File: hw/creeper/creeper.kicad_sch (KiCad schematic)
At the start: 17 parts, among them SW1 EG1218, U1 ATtiny85V-10SU, U2 LIS2DH12TR

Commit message: feat(pcb): v0.7
* added TC2030_AVR pogo debug plug connector
* added isolating resistors to stabilize ISP
* fixed missing connections of battery holder
* added 0R bridge for always-on w/o switch
* moved mounting hole out of case opening
* did manual place and route
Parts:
- added J1: TC2030_AVR, PCM_marbastlib-various:CON_TC2030_outlined, symbol PCM_marbastlib-various:TC2030_AVR
- added RDEC_MISO1, RDEC_MOSI1, RDEC_RST1, RDEC_SCK1: 100R, Resistor_SMD:R_0603_1608Metric_Pad0.98x0.95mm_HandSolder, symbol Device:R_Small
- added R_AON1: 0R, Resistor_SMD:R_0603_1608Metric_Pad0.98x0.95mm_HandSolder, symbol Device:R_Small
- renumbered RPU4 to RPU_CS1, RPU1 to RPU_RST1, RPU3 to RPU_SCL1, RPU2 to RPU_SDA1, R1 to R_BUZ1, R2 to R_LED1, R3 to R_LED2
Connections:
- net +3V: now also J1.2 (VCC), R_AON1.1
- net GND: now also J1.6 (GND); no longer U2.3 (SDO/SA0)
- net INT: now also RDEC_SCK1.1
- net SCL: now also RDEC_MISO1.1
- net SDA: now also RDEC_MOSI1.1
- net ~RESET: now reaches RPU_RST1.1, U1.1 (~{RESET}/PB5)
- net ~RESET: now also RDEC_RST1.1
- net at BT1.1 (+), C_PWR1.1, SW1.3: now also R_AON1.2
- new net: J1.1 (MISO), RDEC_MISO1.2
- new net: J1.4 (MOSI), RDEC_MOSI1.2
- new net: J1.5 (~{RST}), RDEC_RST1.2
- new net: J1.3 (SCK), RDEC_SCK1.2
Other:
- note added: "0.7"
- note added: "2025-AUG-20"
- note removed: "0.6"
- note removed: "2025-JUL-16"
- moved on the sheet: RPU_CS1, RPU_SCL1, RPU_SDA1

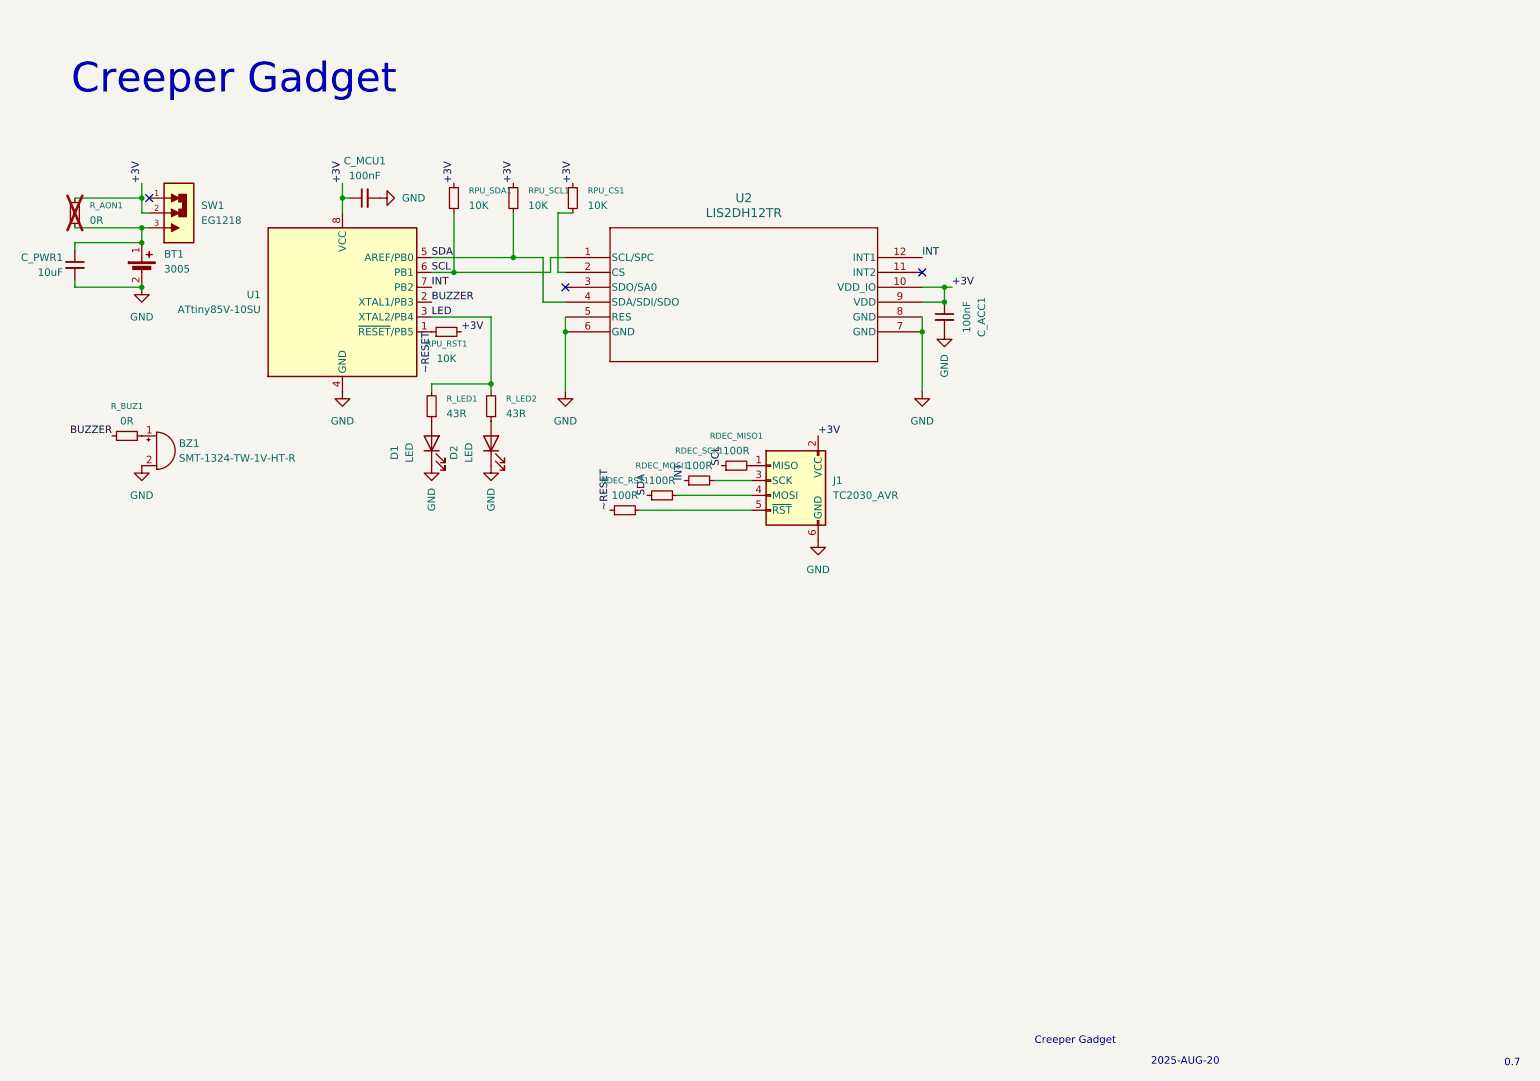
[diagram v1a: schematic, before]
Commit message: feat: rev. 0.10: use analog switch for programmer isolation
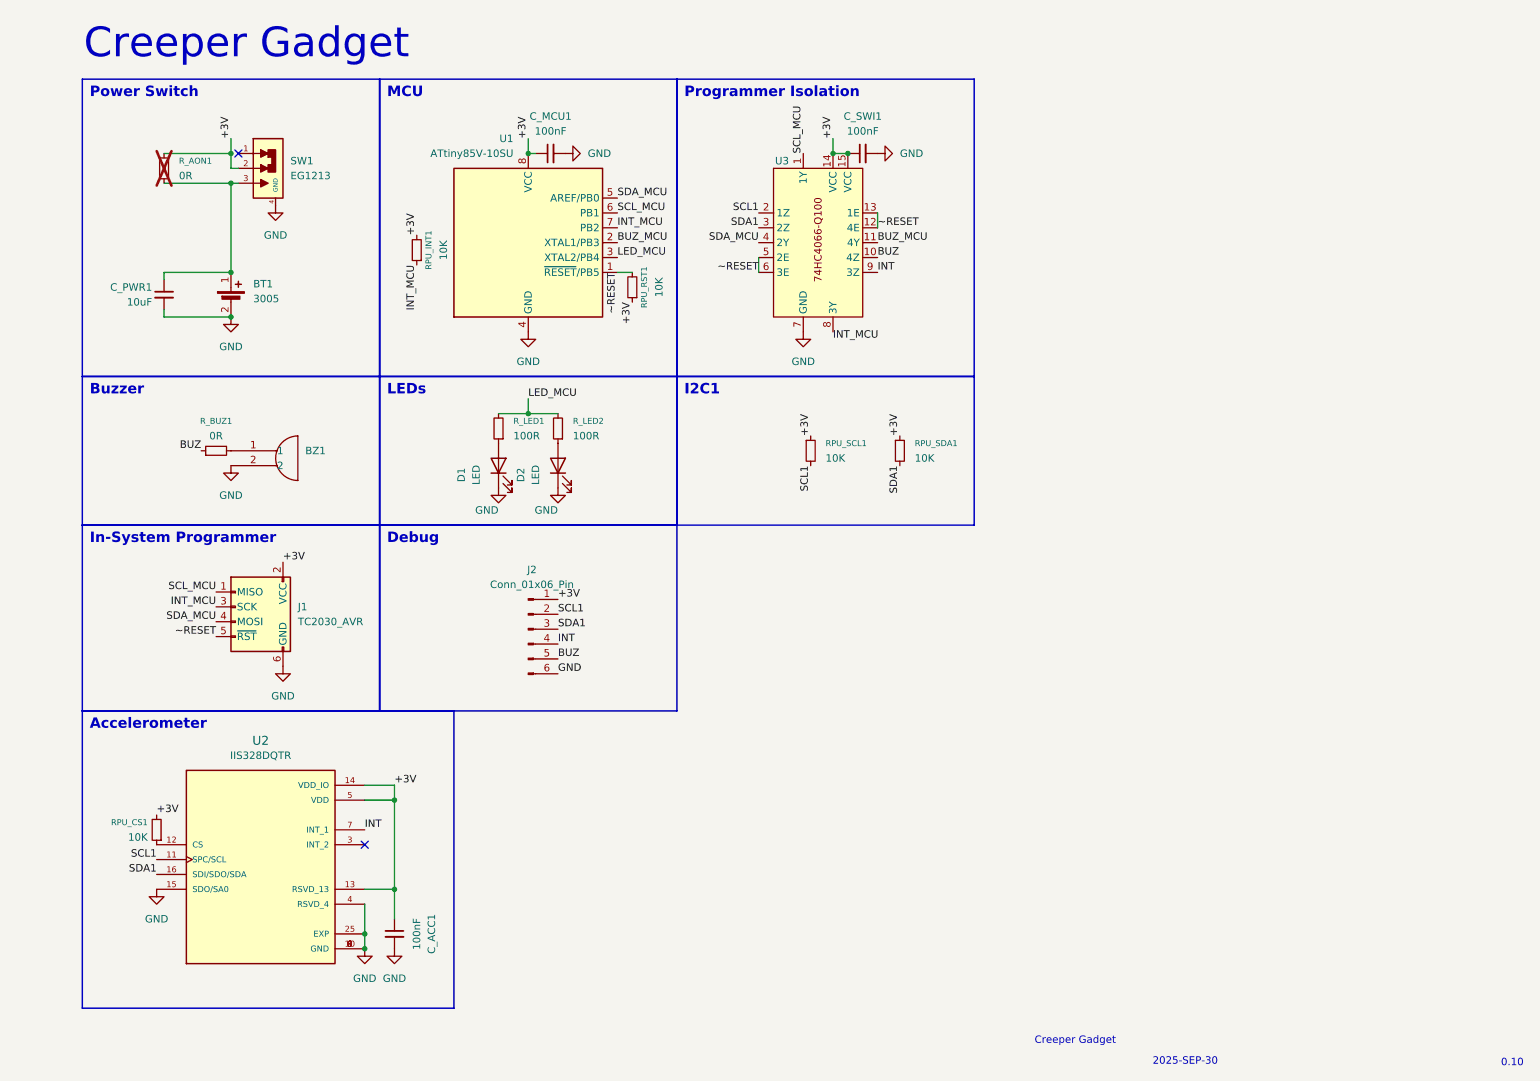
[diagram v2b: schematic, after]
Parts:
- removed RDEC_MISO1, RDEC_MOSI1, RDEC_RST1, RDEC_SCK1: 100R, Resistor_SMD:R_0603_1608Metric_Pad0.98x0.95mm_HandSolder, symbol Device:R_Small
- added C_SWI1: 100nF, creeper:C_0603_1608Metric_Pad1.08x0.95mm_HandSolder, symbol Device:C_Small
- added J2: Conn_01x06_Pin, creeper:PinHeader_1x06_P2.54mm_Vertical, symbol Connector:Conn_01x06_Pin
- added RPU_INT1: 10K, creeper:R_0603_1608Metric_Pad0.98x0.95mm_HandSolder, symbol Device:R_Small
- added U3: ~, creeper:QFN50P300X250X100-15N, symbol creeper:74HC4066-Q100
- BZ1: value SMT-1324-TW-1V-HT-R -> ~; footprint creeper:XDCR_SMT-1324-TW-1V-HT-R -> creeper:XDCR_SMT-0825-S-2-R; symbol Device:Buzzer -> creeper:PT-1241PFQ; MPN SMT-1324-TW-1V-HT-R -> (none); Manufacturer PUI Audio, Inc. -> (none); SolderJoints 2 -> (none)
- C_ACC1, C_MCU1: footprint Capacitor_SMD:C_0603_1608Metric_Pad1.08x0.95mm_HandSolder -> creeper:C_0603_1608Metric_Pad1.08x0.95mm_HandSolder
- C_PWR1: footprint Capacitor_SMD:C_0805_2012Metric_Pad1.18x1.45mm_HandSolder -> creeper:C_0805_2012Metric_Pad1.18x1.45mm_HandSolder
- RPU_CS1, RPU_RST1, RPU_SCL1, RPU_SDA1, R_AON1, R_BUZ1: footprint Resistor_SMD:R_0603_1608Metric_Pad0.98x0.95mm_HandSolder -> creeper:R_0603_1608Metric_Pad0.98x0.95mm_HandSolder
- R_LED1, R_LED2: value 43R -> 100R; footprint Resistor_SMD:R_0603_1608Metric_Pad0.98x0.95mm_HandSolder -> creeper:R_0603_1608Metric_Pad0.98x0.95mm_HandSolder
- SW1: value EG1218 -> EG1213; footprint creeper:SW_EG1218 -> creeper:SW_EG1213; symbol creeper:EG1218 -> creeper:EG1213
- U1: footprint Package_SO:SOIC-8_5.3x5.3mm_P1.27mm -> creeper:SOIC-8_5.3x5.3mm_P1.27mm
- U2: value LIS2DH12TR -> IIS328DQTR; footprint creeper:LGA-12_STM -> creeper:IIS328DQTR_QFN50P400X400X185-25N; symbol creeper:LIS2DH12TR -> creeper:IIS328DQTR; A_MAX (none) -> 1.85; B_MAX (none) -> 0.3; B_MIN (none) -> 0.2; B_NOM (none) -> 0.25; Check_prices (none) -> https://www.snapeda.com/parts/IIS328DQTR/STMicroelectronics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; D2_NOM (none) -> 2.3; D_MAX (none) -> 4.0; D_MIN (none) -> 4.0; D_NOM (none) -> 4.0; Description_1 (none) -> Accelerometer X, Y, Z Axis ±2g, 4g, 8g 25Hz ~ 500Hz 24-QFN 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; DigiKey_Part_Number (none) -> 497-15701-1-ND; E2_NOM (none) -> 2.3; ENOM (none) -> 0.5; E_MAX (none) -> 4.0; E_MIN (none) -> 4.0; E_NOM (none) -> 4.0; L_MAX (none) -> 0.45; L_MIN (none) -> 0.35; L_NOM (none) -> 0.4; MANUFACTURER (none) -> ST Microelectronics; MAXIMUM_PACKAGE_HEIGHT (none) -> 1.85mm; MF (none) -> STMicroelectronics; MP (none) -> IIS328DQTR; MPN LIS2DH12TR -> (none); Manufacturer STMicroelectronics -> (none); PARTREV (none) -> 3; PIN_COUNT_D (none) -> 6.0; PIN_COUNT_E (none) -> 6.0; Package (none) -> QFN-24 STMicroelectronics; STANDARD (none) -> IPC 7351B; SnapEDA_Link (none) -> https://www.snapeda.com/parts/IIS328DQTR/STMicroelectronics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; SolderJoints 12 -> (none)
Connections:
- net +3V: now also RPU_CS1.2, RPU_RST1.1, U2.13 (RSVD_13), U2.14 (VDD_IO), U2.5 (VDD), C_SWI1.1, J2.1 (Pin_1), RPU_INT1.2, U3.14 (VCC), U3.15 (VCC); no longer RPU_CS1.1, RPU_RST1.2, U2.10 (VDD_IO), U2.9 (VDD)
- net GND: now also SW1.4 (GND), U2.10 (GND), U2.15 (SDO/SA0), U2.25 (EXP), U2.4 (RSVD_4), U2.9 (GND), C_SWI1.2, J2.6 (Pin_6), U3.7 (GND); no longer U2.5 (RES), U2.7 (GND)
- net INT: now also U2.7 (INT_1), J2.4 (Pin_4), U3.9 (3Z); no longer U1.7 (PB2), U2.12 (INT1)
- net ~RESET: now also J1.5 (~{RST}), RPU_RST1.2, U3.12 (4E), U3.13 (1E), U3.5 (2E), U3.6 (3E); no longer RPU_RST1.1
- net SCL_MCU: now reaches J1.1 (MISO)
- net SCL_MCU: now also U1.6 (PB1), U3.1 (1Y)
- net SDA_MCU: now reaches J1.4 (MOSI)
- net SDA_MCU: now also U1.5 (AREF/PB0), U3.4 (2Y)
- net INT_MCU: now reaches J1.3 (SCK)
- net INT_MCU: now also U1.7 (PB2), RPU_INT1.1, U3.8 (3Y)
- net SCL1: now reaches U2.11 (SPC/SCL)
- net SCL1: now also RPU_SCL1.2, J2.2 (Pin_2), U3.2 (1Z)
- net BUZZER renamed BUZ
- net BUZ: now also J2.5 (Pin_5), U3.10 (4Z); no longer U1.2 (XTAL1/PB3)
- net LED renamed LED_MCU
- removed net SCL: RPU_SDA1.2, U1.6 (PB1), U2.1 (SCL/SPC)
- removed net SDA: RPU_SCL1.2, U1.5 (AREF/PB0), U2.4 (SDA/SDI/SDO)
- new net: RPU_CS1.1, U2.12 (CS)
- new net BUZ_MCU: U1.2 (XTAL1/PB3), U3.11 (4Y)
- new net SDA1: J2.3 (Pin_3), RPU_SDA1.2, U2.16 (SDI/SDO/SDA), U3.3 (2Z)
- no-connect marks 3 -> 2
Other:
- note added: "0.10"
- note added: "2025-SEP-30"
- note added: "Accelerometer"
- note added: "Buzzer"
- note added: "Debug"
- note added: "I2C1"
- note added: "In-System Programmer"
- note added: "LEDs"
- note added: "MCU"
- note added: "Power Switch"
- note added: "Programmer Isolation"
- note removed: "0.7"
- note removed: "2025-AUG-20"
- moved on the sheet: BT1, C_ACC1, C_MCU1, C_PWR1, D1, D2, J1, RPU_CS1, RPU_RST1, RPU_SCL1, RPU_SDA1, R_AON1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

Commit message: feat: v0.11: replace accelerometer with optional spring vibration sensor
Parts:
- added RPU_SVS1: 10K, creeper:R_0603_1608Metric_Pad0.98x0.95mm_HandSolder, symbol Device:R
- added SVS1: SW_Push, creeper:SW_180xxP_Spring_Vibration_Sensor, symbol Switch:SW_Push
- BZ1, J1, R_AON1: now left out of the parts list
- J2: now not fitted; now left out of the parts list
- SW1: Check_prices https://www.snapeda.com/parts/EG1218/E-Switch/view-part/?re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 -> https://www.snapeda.com/parts/EG1213/E-Switch/view-part/?re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; MP EG1218 -> EG1213; MPN EG1218 -> EG1213; PURCHASE-URL https://pricing.snapeda.com/search/part/EG1218/?ref=eda -> https://pricing.snapeda.com/search/part/EG1213/?ref=eda; SnapEDA_Link https://www.snapeda.com/parts/EG1218/E-Switch/view-part/?re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 -> https://www.snapeda.com/parts/EG1213/E-Switch/view-part/?re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; SolderJoints (none) -> 5
- U2: MANUFACTURER ST Microelectronics -> (none); MPN (none) -> IIS328DQTR; Manufacturer (none) -> ST Microelectronics; SolderJoints (none) -> 25; now not fitted
- U3: MPN (none) -> 74HC4066BQ-Q100,11; Manufacturer (none) -> Nexperia USA Inc.; SolderJoints (none) -> 15; now not fitted
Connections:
- net +3V: now also RPU_SVS1.2
- net INT: now also SVS1.1
- new net: RPU_SVS1.1, SVS1.2
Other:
- note added: "0.11"
- note added: "2025-OCT-19"
- note added: "Spring vibration sensor"
- note removed: "0.10"
- note removed: "2025-SEP-30"
- moved on the sheet: RPU_SCL1, RPU_SDA1

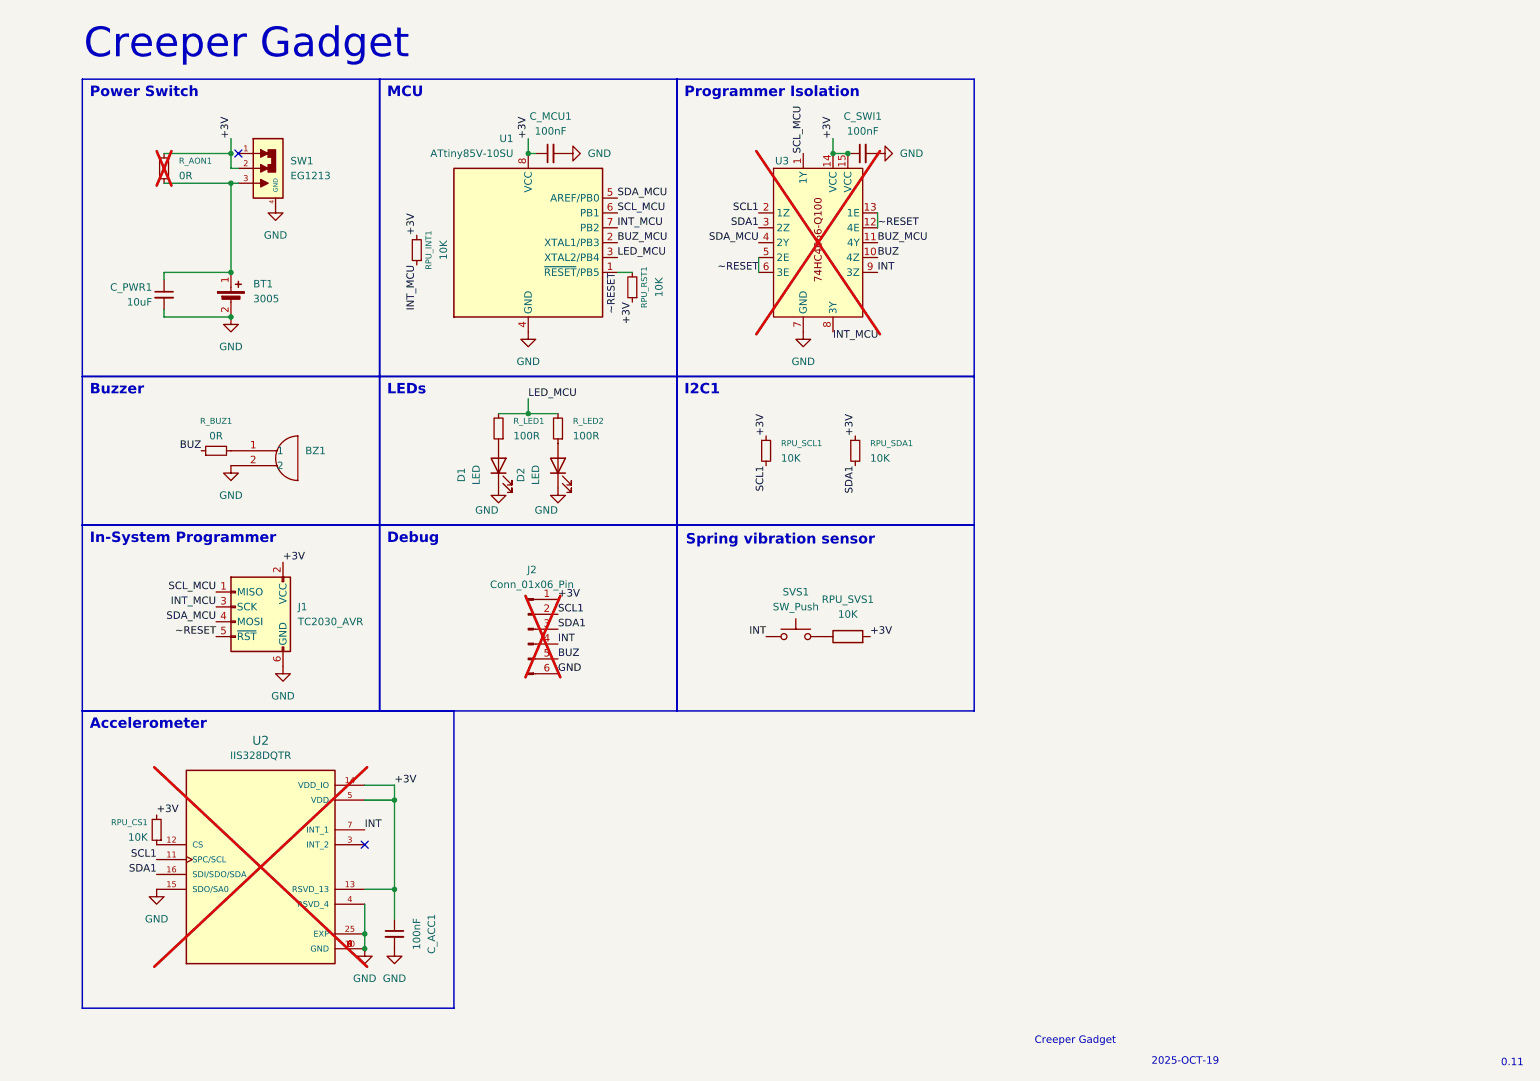
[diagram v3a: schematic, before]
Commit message: fix(sch+pcb): update footprints, reset DNP
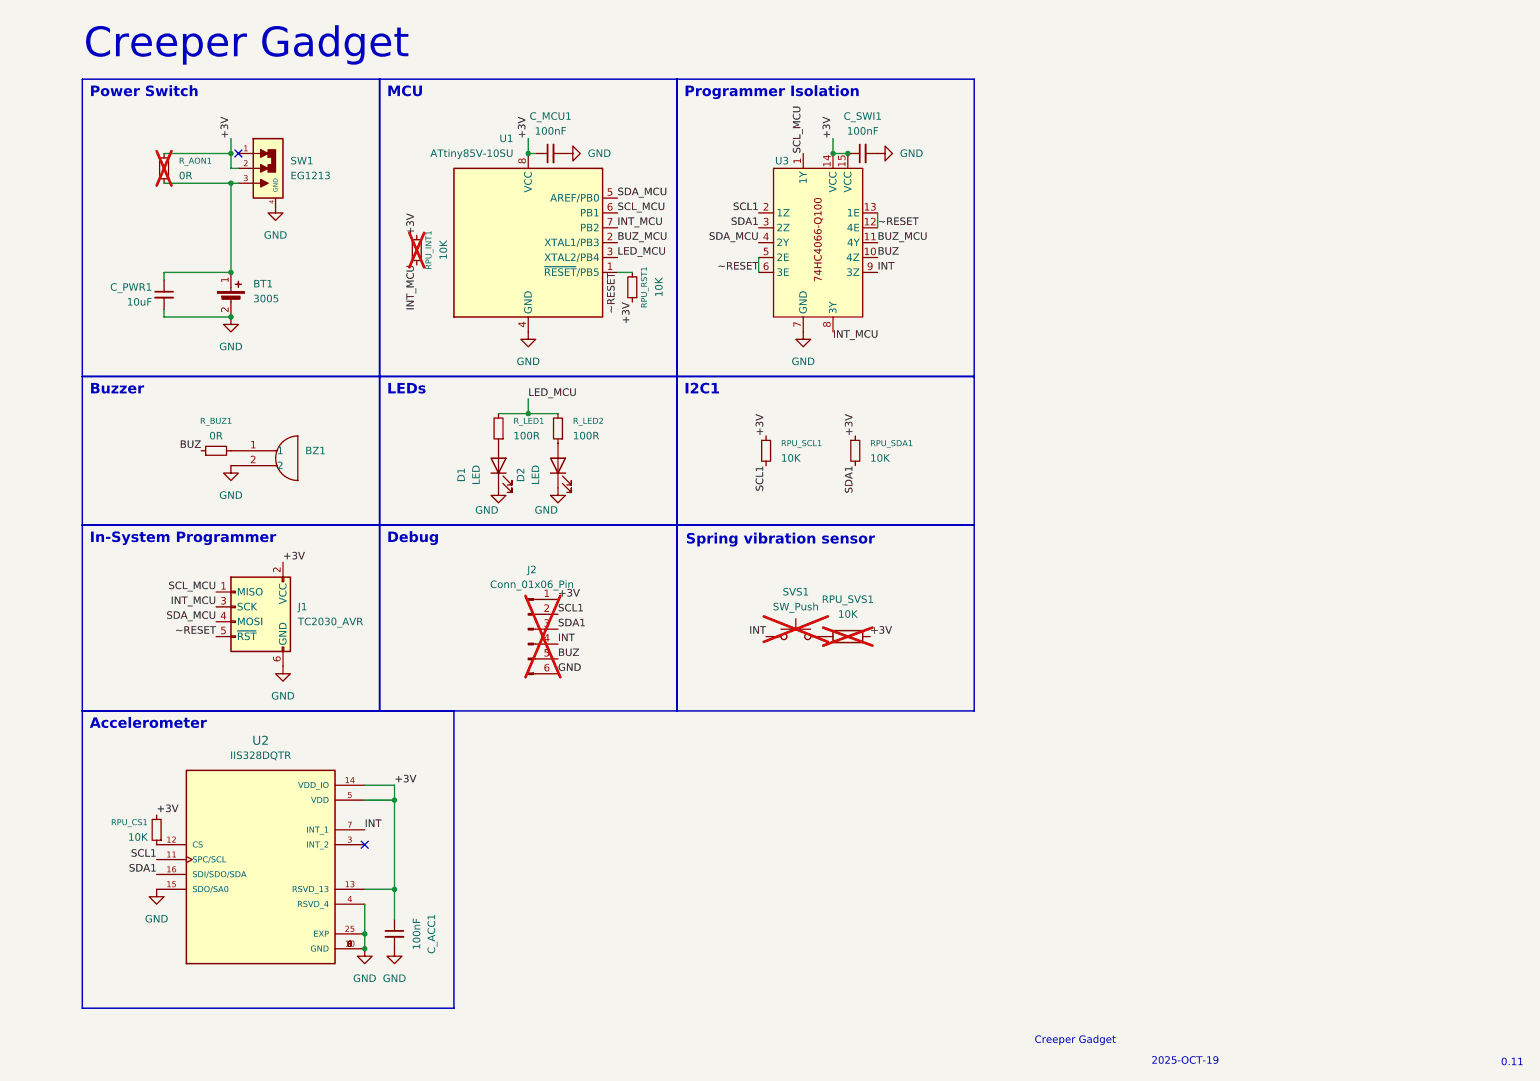
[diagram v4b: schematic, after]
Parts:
- RPU_INT1, RPU_SVS1, SVS1: now not fitted
- U2, U3: now fitted
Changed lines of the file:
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@@
 		(in_bom yes)
 		(on_board yes)
-		(dnp no)
+		(dnp yes)
 		(fields_autoplaced yes)
 		(property "Reference" "SVS1"
@@
 		(in_bom yes)
 		(on_board yes)
-		(dnp yes)
+		(dnp no)
 		(property "Reference" "U3"
 			(at 143.764 39.37 0)
@@
 		(in_bom yes)
 		(on_board yes)
-		(dnp no)
+		(dnp yes)
 		(property "Reference" "RPU_INT1"
 			(at 84.582 54.61 90)
@@
 		(in_bom yes)
 		(on_board yes)
-		(dnp no)
+		(dnp yes)
 		(fields_autoplaced yes)
 		(property "Reference" "RPU_SVS1"
@@
 		(in_bom yes)
 		(on_board yes)
-		(dnp yes)
+		(dnp no)
 		(fields_autoplaced yes)
 		(property "Reference" "U2"
